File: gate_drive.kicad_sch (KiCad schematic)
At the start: 233 parts, among them J19 Conn_01x03, J20 Conn_01x03, Q1 Q_PNP_BEC, Q2 Q_PNP_BEC, Q3 Q_PNP_BEC, Q4 Q_PNP_BEC, Q5 Q_PNP_BEC, Q6 Q_PNP_BEC, U1 EG3113, U14 INA193, U2 EG3113, U20 INA193, U21 INA193, U22 INA193, U35 INA193, U36 INA826, U37 INA193, U38 INA826, U39 INA193, U4 EG3113, U40 INA826, U41 INA193, U42 INA826, U5 EG3113, U7 EG3113, U8 EG3113

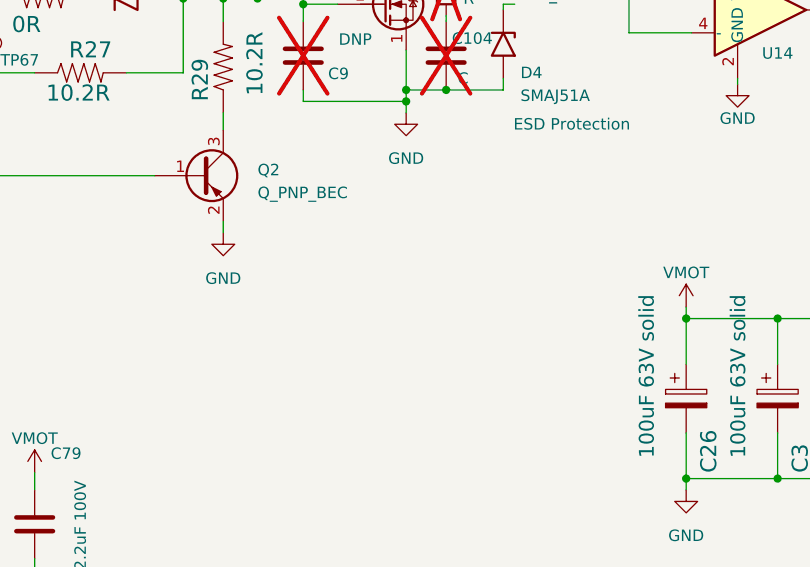
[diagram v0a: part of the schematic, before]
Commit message: Added test point labels to all bridge test points, regenerated STEP file and schematic PDF
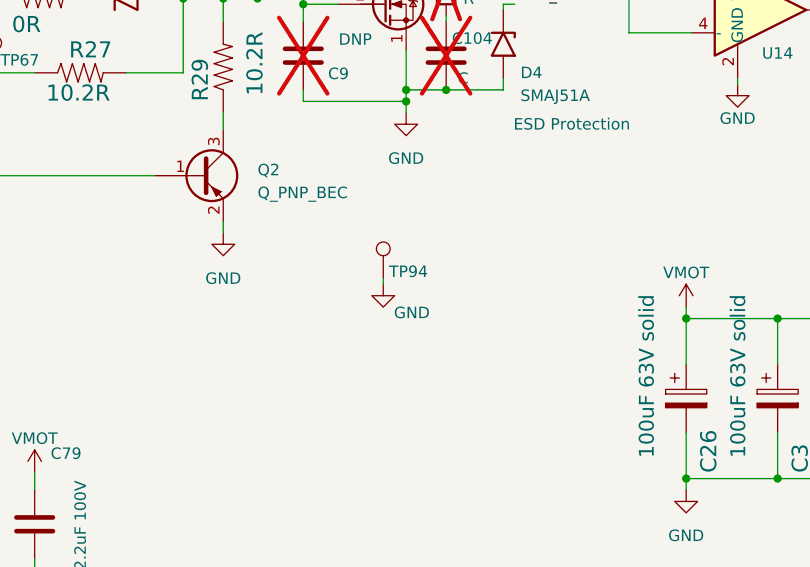
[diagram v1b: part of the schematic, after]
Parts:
- added TP94: TestPoint, TestPoint:TestPoint_Pad_D1.5mm, symbol Connector:TestPoint
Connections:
- net GND: now also TP94.1
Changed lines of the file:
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@@
     (stroke (width 0) (type default))
   )
+  (wire (pts (xy 295.275 221.615) (xy 295.275 220.98))
+    (stroke (width 0) (type default))
+  )
   (wire (pts (xy 48.895 52.705) (xy 50.8 52.705))
     (stroke (width 0) (type default))
@@
     )
   )
+  (symbol (lib_id "Connector:TestPoint") (at 295.275 220.98 0) (unit 1)
+    (in_bom no) (on_board yes) (dnp no)
+    (property "Reference" "TP94" (at 295.91 220.218 0)
+      (effects (font (size 1.27 1.27)) (justify left))
+    )
+    (property "Value" "TestPoint" (at 297.18 219.583 0)
+      (effects (font (size 1.27 1.27)) (justify left) hide)
+    )
+    (property "Footprint" "TestPoint:TestPoint_Pad_D1.5mm" (at 300.355 220.98 0)
+      (effects (font (size 1.27 1.27)) hide)
+    )
+    (property "Datasheet" "~" (at 300.355 220.98 0)
+      (effects (font (size 1.27 1.27)) hide)
+    )
+    (pin "1")
+    (instances
+      (project "RP2040_motor"
+        (path "/10ff4ace-8dac-45ce-94a5-ae8ae7d42914/a091b038-73b8-4e3d-85bf-957d7c13689e"
+          (reference "TP94") (unit 1)
+        )
+      )
+    )
+  )
   (symbol (lib_id "power:GND") (at 249.555 71.12 0) (unit 1)
     (in_bom yes) (on_board yes) (dnp no) (fields_autoplaced)
@@
         )
       )
+    )
+  )
+  (symbol (lib_id "power:GND") (at 295.275 221.615 0) (unit 1)
+    (in_bom yes) (on_board yes) (dnp no)
+    (property "Reference" "#PWR0292" (at 295.275 227.965 0)
+      (effects (font (size 1.27 1.27)) hide)
+    )
+    (property "Value" "GND" (at 298.45 224.79 0)
+      (effects (font (size 1.27 1.27)))
+    )
+    (property "Footprint" "" (at 295.275 221.615 0)
+      (effects (font (size 1.27 1.27)) hide)
+    )
+    (property "Datasheet" "" (at 295.275 221.615 0)
+      (effects (font (size 1.27 1.27)) hide)
+    )
+    (pin "1")
+    (instances
+      (project "RP2040_motor"
+        (path "/10ff4ace-8dac-45ce-94a5-ae8ae7d42914/a091b038-73b8-4e3d-85bf-957d7c13689e"
+          (reference "#PWR0292") (unit 1)
+        )
+      )

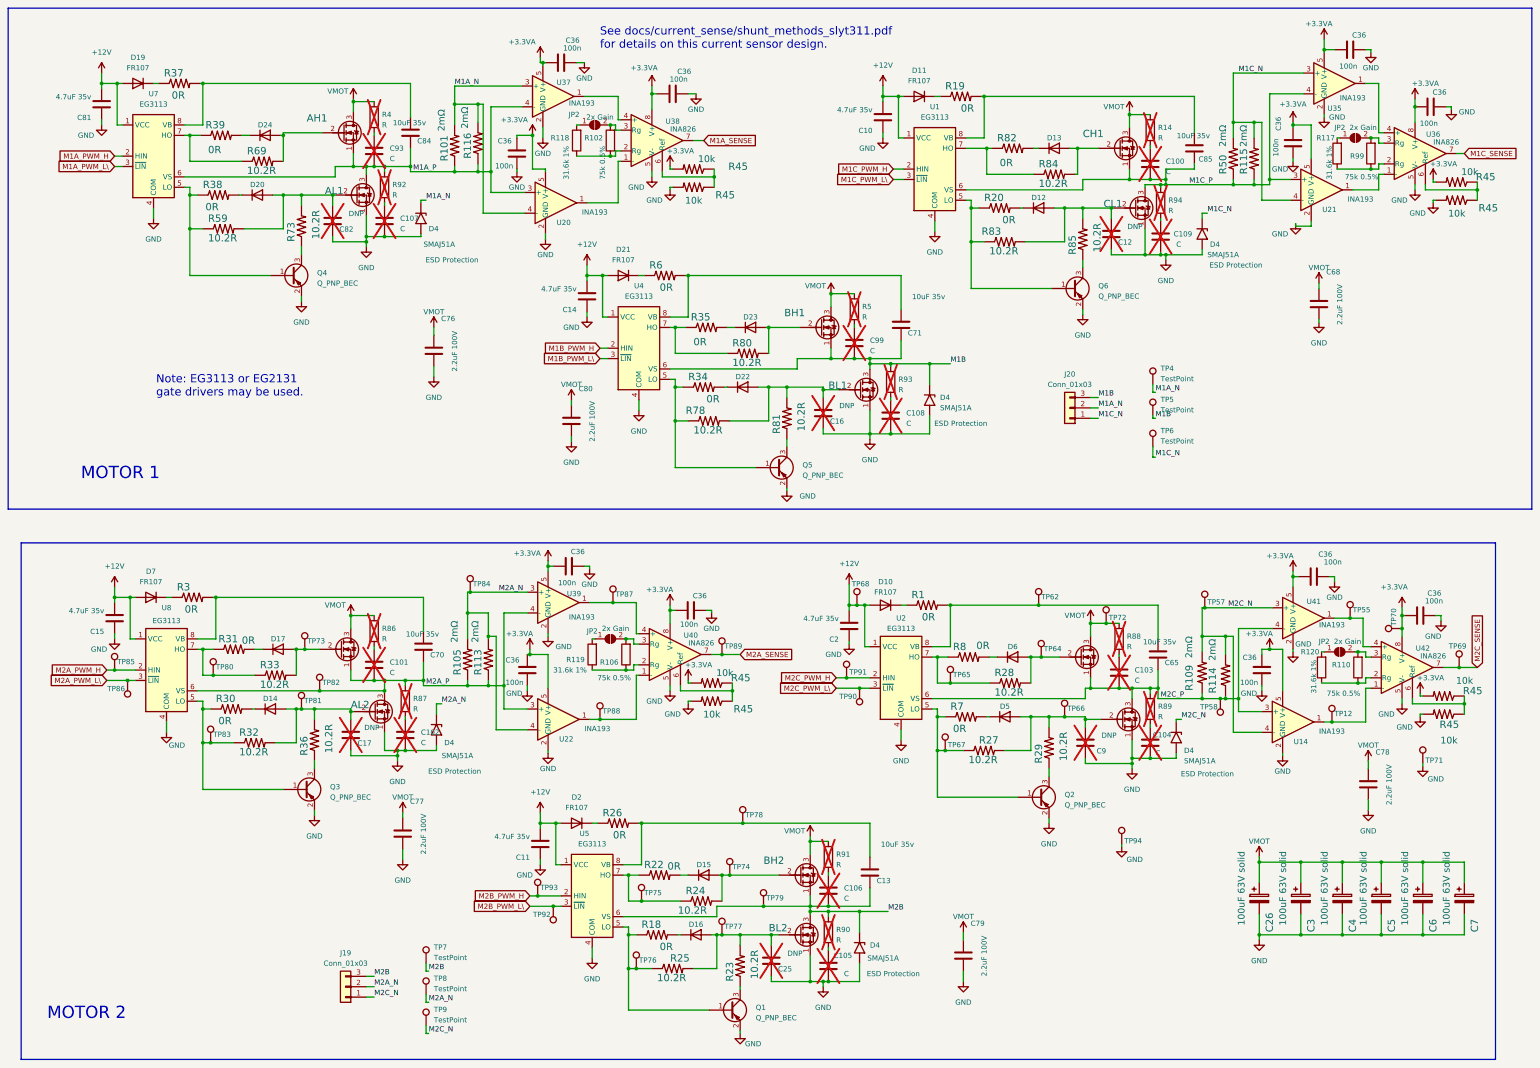
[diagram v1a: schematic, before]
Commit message: Changed current sense circuit as per recommendation. Added extra combined AUX port.
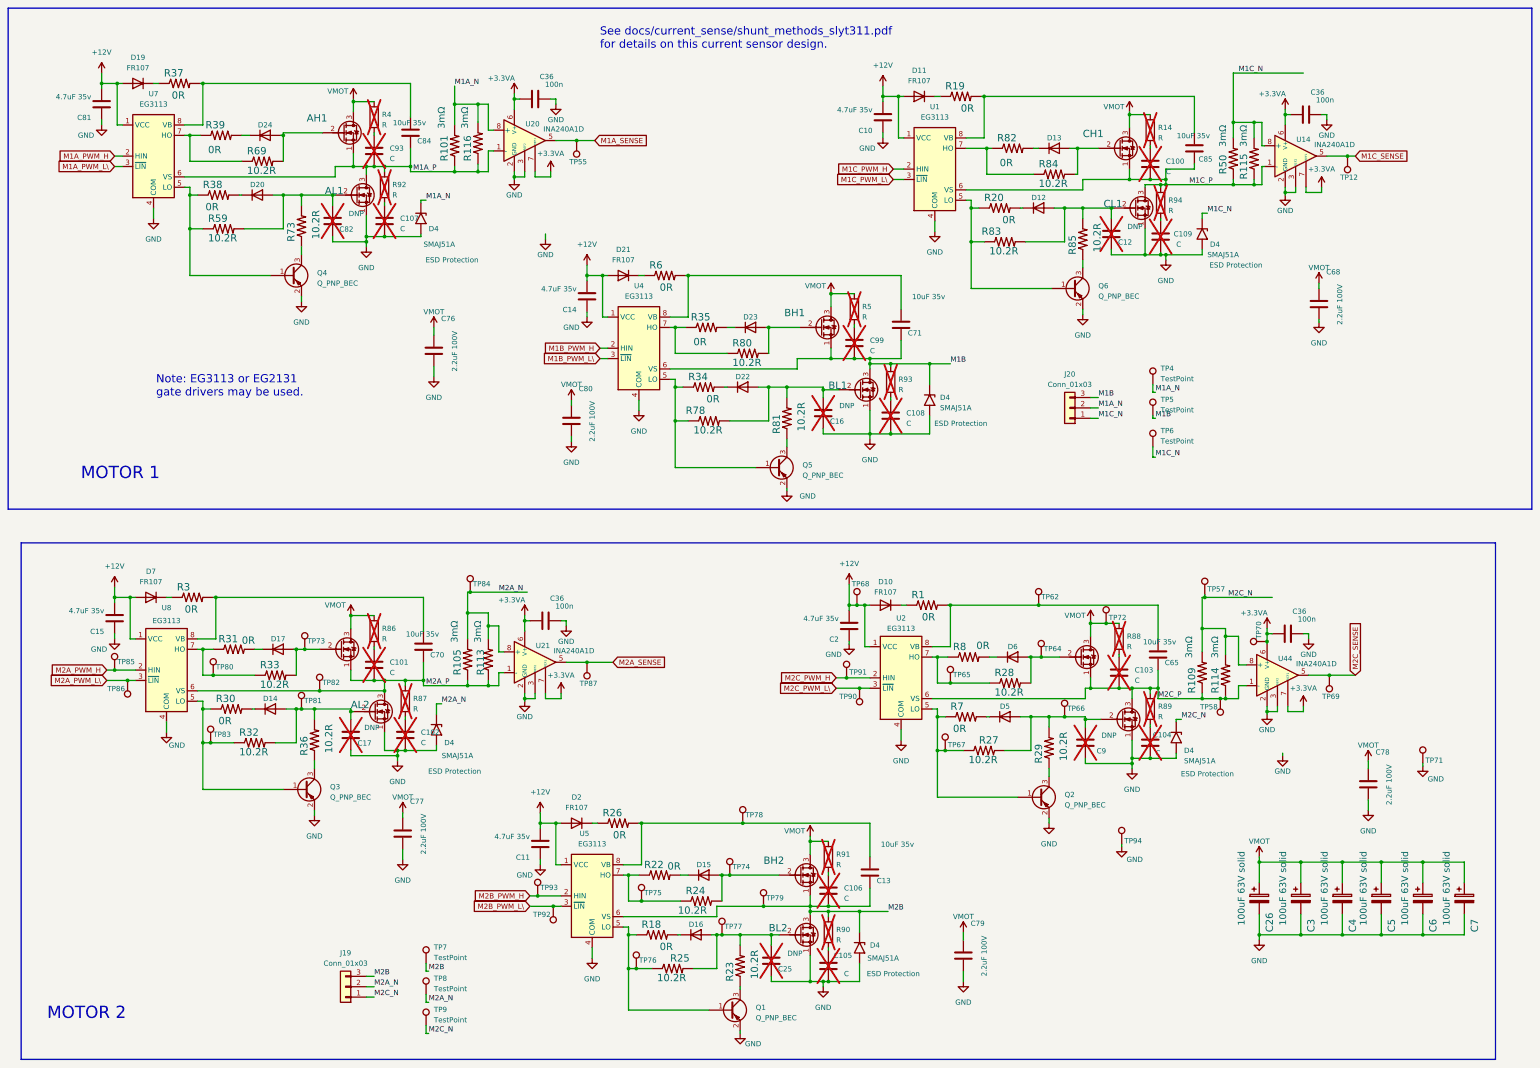
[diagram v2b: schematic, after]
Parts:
- removed C36 (x11): 100n, Capacitor_SMD:C_0603_1608Metric, symbol Device:C
- removed JP2 (x4): SolderJumper_2_Open, Jumper:SolderJumper-2_P1.3mm_Open_RoundedPad1.0x1.5mm, symbol Jumper:SolderJumper_2_Open
- removed R102, R106, R110, R99: 75k 0.5%, Resistor_SMD:R_0603_1608Metric, symbol Device:R
- removed R117, R118, R119, R120: 31.6k 1%, Resistor_SMD:R_0603_1608Metric, symbol Device:R
- removed R45 (x8): 10k, Resistor_SMD:R_0603_1608Metric, symbol MotorController:TAYLOR_RESISTOR
- removed TP88, TP89: TestPoint, TestPoint:TestPoint_Pad_D1.5mm, symbol Connector:TestPoint
- removed U14, U20, U21, U22, U35, U37, U39, U41: INA193, Package_TO_SOT_SMD:SOT-23-5, symbol Amplifier_Current:INA193
- removed U36, U38, U40, U42: INA826, Package_SO:SO-8_3.9x4.9mm_P1.27mm, symbol motor_parts:INA826
- added C36 (x3): 100n, Capacitor_SMD:C_0603_1608Metric, symbol Device:C
- added U14, U20, U21, U44: INA240A1D, Package_SO:SOIC-8_3.9x4.9mm_P1.27mm, symbol Amplifier_Current:INA240A1D
- R101, R105, R109, R113, R114, R115, R116, R50: value 2mΩ -> 3mΩ; LCSC C695813 -> C2688862
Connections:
- net +3.3VA: now also C36.1, C36.1, C36.1, U14.6 (V+), U14.7 (REF1), U20.6 (V+), U20.7 (REF1), U21.6 (V+), U21.7 (REF1), U44.6 (V+), U44.7 (REF1)
- net GND: now also C36.2, C36.2, C36.2, U14.2 (GND), U14.3 (REF2), U14.4 (GND), U20.2 (GND), U20.3 (REF2), U20.4 (GND), U21.2 (GND), U21.3 (REF2), U21.4 (GND), U44.2 (GND), U44.3 (REF2), U44.4 (GND)
- net M1A_N: now also U20.8 (+)
- net M1A_P: now also U20.1 (-)
- net M1A_SENSE: now also TP55.1, U20.5
- net M1C_N: now also U14.8 (+)
- net M1C_P: now also U14.1 (-)
- net M1C_SENSE: now also TP12.1, U14.5
- net M2A_N: now also U21.8 (+)
- net M2A_P: now also U21.1 (-)
- net M2A_SENSE: now also TP87.1, U21.5
- net M2C_N: now also U44.8 (+)
- net M2C_P: now also U44.1 (-)
- net M2C_SENSE: now also U44.5
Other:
- moved on the sheet: C36, TP57, TP69, TP70
